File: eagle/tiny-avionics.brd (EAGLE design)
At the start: 65.8 x 25.4 mm, 62 parts, among them J1 USB-MICROB, J3 JST-PH-2-SMT-RA, U1 LP5907, U2 M25PX16, U3 LSM6DS3, U4 BQ21040, U5 LTC1998, U6 ATMEGA32U4-AU, X1 8MHz

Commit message: Went through a few of the issues Andrew raised.  Still some that need to be addressed.
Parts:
- U$1: value THERMISTOR-SMD0603 -> 10k B25/50=3375k
- moved TP13 3.21 mm to (10.3, 23.9)
- moved JP2 2.29 mm to (29.2, 3.94)
- moved C11 1.83 mm to (49.0, 1.37)
- moved C12 0.98 mm to (33.8, 2.52), turned to 270 degrees
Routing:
- net MOSI: track 39.4 -> 32.2 mm, vias 2 -> 3
- net MISO: track 26.7 -> 29.8 mm, vias 1 -> 2
- net MEM_EN: track 46.7 -> 48.8 mm
- net D+: track 35.4 -> 33.6 mm
- net GND: track 1.06 -> 2.83 mm, vias 112 -> 114
- net CLK: track 51.8 -> 50.1 mm
- net VCC: track 131.8 -> 133.3 mm
- net N$13: track 30.7 -> 32.1 mm
- net N$3: track 48.2 -> 49.1 mm
- net N$2: track 11.8 -> 11.1 mm
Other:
- board text added: "OFF"
- board text added: "ON"
- board text removed: "1 MISO"

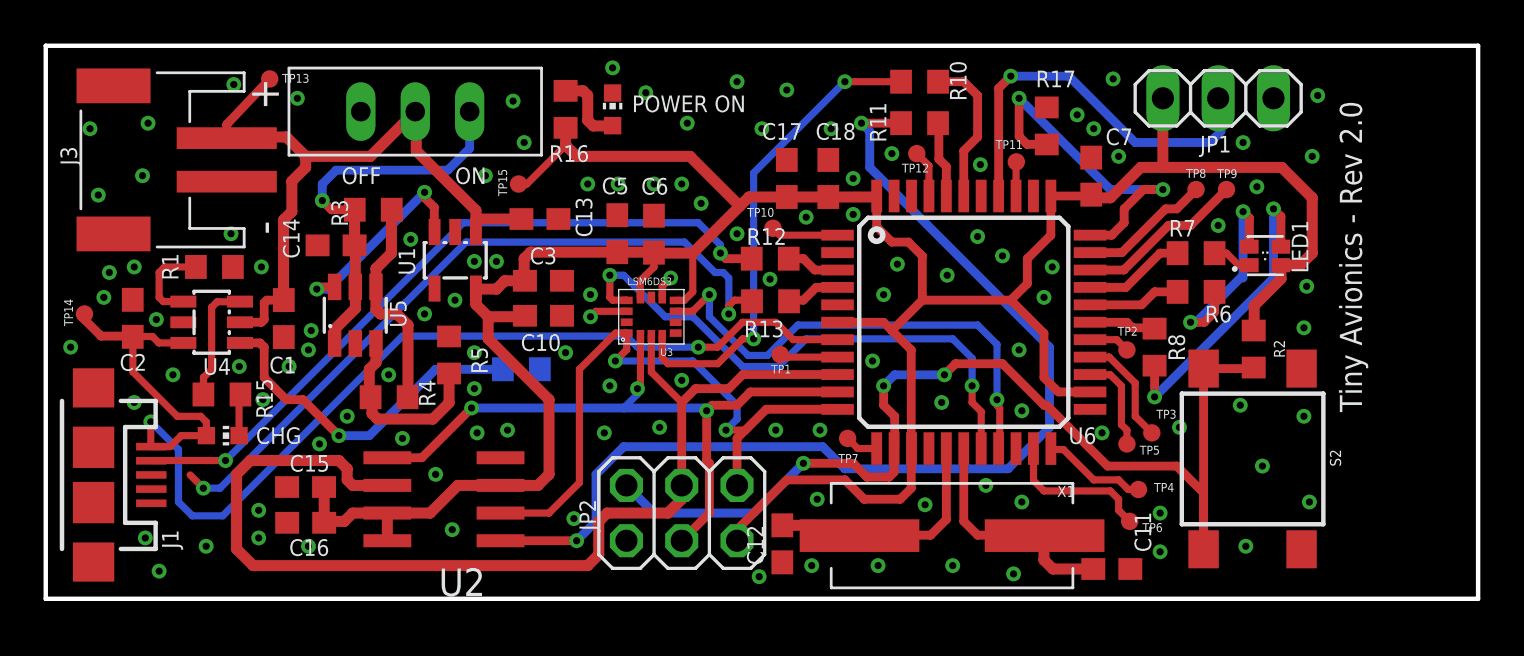
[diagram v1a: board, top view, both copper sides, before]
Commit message: Finished layout rework from 2nd design review.
Still left to do:
-Change 0603 footprints to RCL custom library 0603s
-Additional schematic work
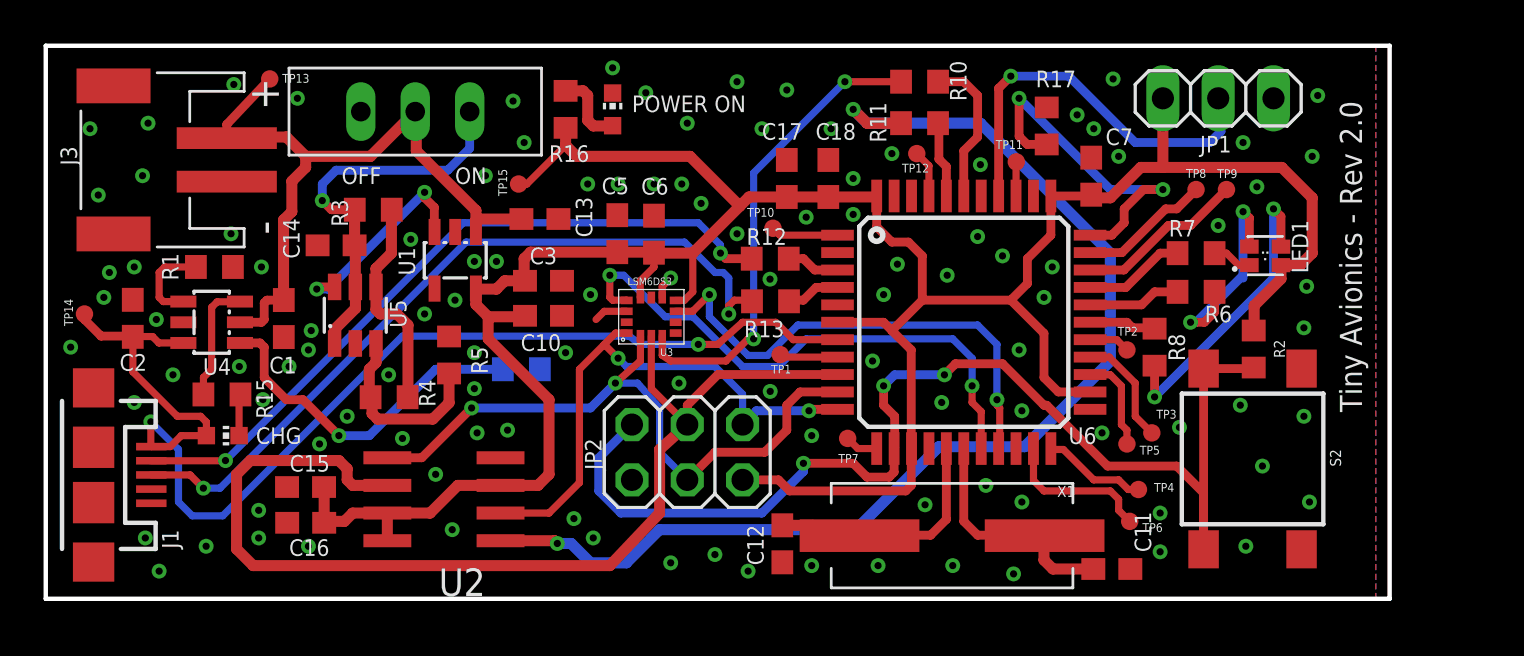
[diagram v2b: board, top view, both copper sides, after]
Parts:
- moved JP2 2.81 mm to (29.5, 6.73)
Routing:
- net MEM_EN: track 48.8 -> 54.2 mm
- net N$3: track 49.1 -> 54.2 mm
- net MISO: track 29.8 -> 25.6 mm
- net VCC: track 133.3 -> 131.2 mm
- net MOSI: track 32.2 -> 30.2 mm, vias 3 -> 2
- net D+: track 33.6 -> 35.4 mm
- net GND: track 2.83 -> 2.63 mm, vias 114 -> 112
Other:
- board size 65.8 x 25.4 mm -> 61.7 x 25.4 mm

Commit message: Fixed remaining design rev issues. Slightly thinner pads for LSM6DS0 to comply with OshPark DRC.
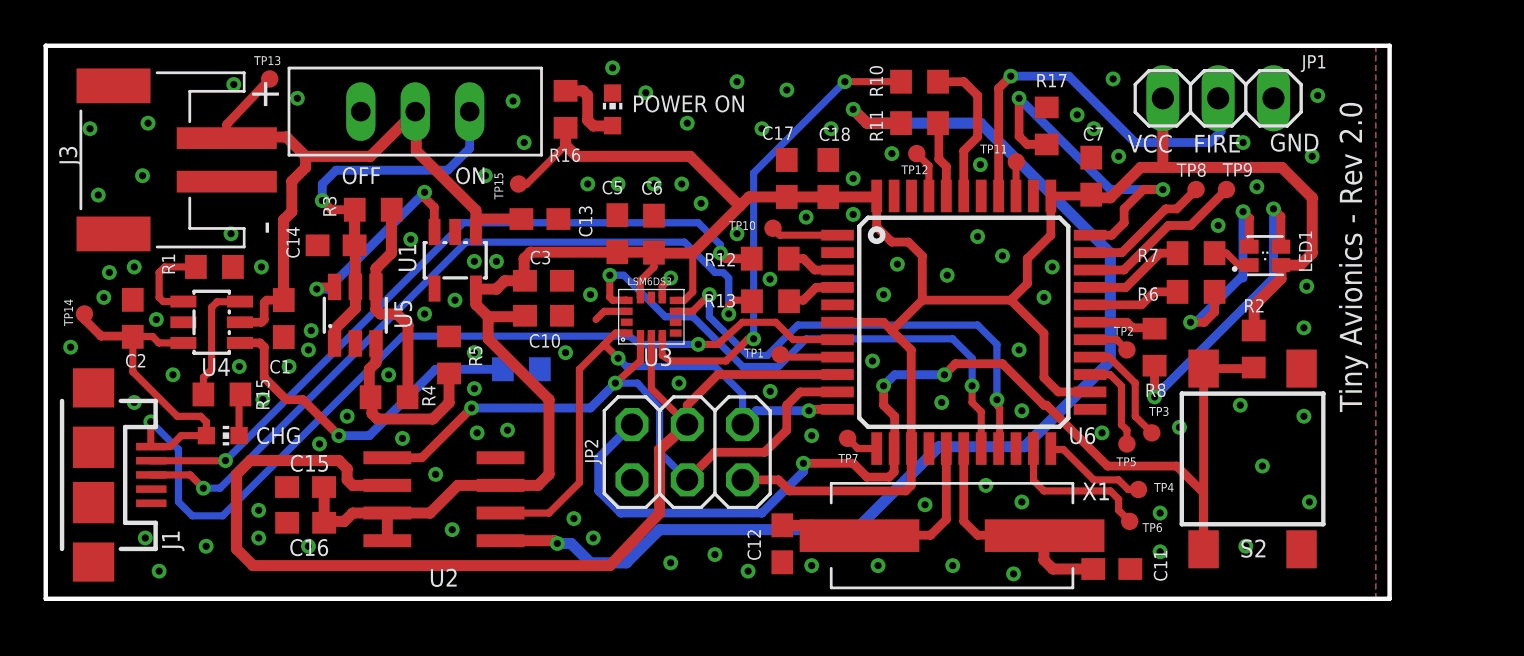
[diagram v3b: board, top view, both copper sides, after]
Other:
- board text added: "FIRE"
- board text added: "GND"
- board text added: "VCC"
